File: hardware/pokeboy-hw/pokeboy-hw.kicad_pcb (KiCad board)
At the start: 4 copper layers, 79.4 x 119.4 mm, 110 parts, among them J1 USB Micro-B data/power, J2 LiPo 1S + / NTC / -, J3 POWER SWITCH PADS, J4 8 OHM SPEAKER PADS, J5 EA TFT020-23AINN RGB666, J6 UART TEST PADS, J7 RECOVERY SHORT PADS, J8 RESET SHORT PADS, J9 104031-0811, SW1 EVQ-P1905M, SW2 EVQ-P1905M, SW3 EVQ-P1905M, SW4 EVQ-P1905M, SW5 B3AL-1001P, SW6 B3AL-1001P, SW7 EVQ-P2B02B, SW8 EVQ-P2B02B, U1 OSD3358-1G-ISM, U2 BQ24074RGT, U3 TPS63802DLAR, U4 TPS62162DSG, U5 TPS61165DRV, U6 MAX98357AETE+T, U7 TPD2EUSB30, Y1 24 MHz

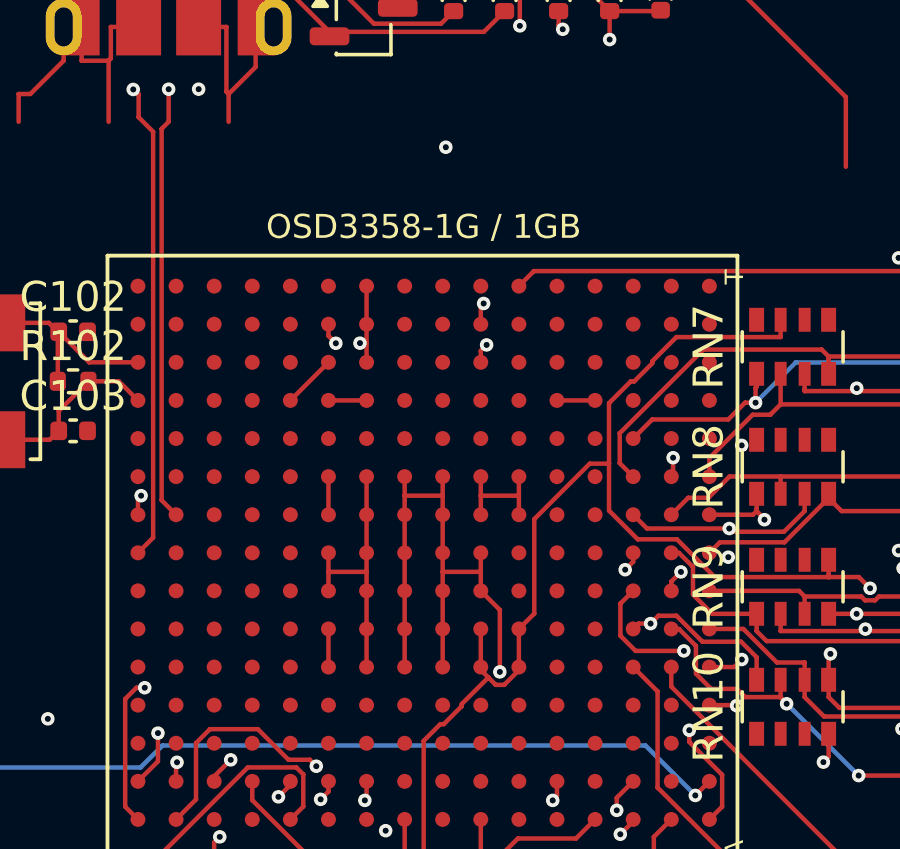
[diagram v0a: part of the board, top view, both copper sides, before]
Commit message: hw: close the Octavo checklist copper items
- SYS_VOUT bulk (PD4, was mandatory-and-missing): C107-C109, three 22 uF 0402
  (same GRM155R61A226ME11D as C7/C8, 66 uF nominal to survive DC-bias derating)
  placed below U1 at y=9.7, fed by a 0.3 mm F.Cu trunk down the col-6/7 ball
  gap from the existing SYS_VOUT interlink; GND pads land in the F.Cu pour.
- VIN_BAT (P8/R8/T8) strapped to PMIC_BAT_SENSE (N7) as new net /VIN_BAT;
  VIN_USB (P9/R9/T9) tied to GND via the N9 ball - Table 13 Use Case 4.
- EEPROM_WP (M2) tied to GND.
- 12 GND stitching vias added beside DGND balls under U1 (was 2 in the whole
  field), each collision-checked on all four layers; drill 227 -> 239 hits.
- U1's schematic symbol gains the 8 previously-floating pins; 3 cap symbols
  added; netlist and board verified identical net for net.

DRC 0 errors / 0 unconnected / 37 warnings (one new cosmetic silk-over-copper
from the cap refs). ERC 0 errors / 4 baseline warnings. Fab outputs, CPL (103
placements), BOM, renders, copper SVGs, STEP, schematic PDF regenerated.

Software note carried in HANDOVER: disable the TPS65217 charger (external
BQ24074 charges the cell) and cap the sustained OPP per the thermal plan.
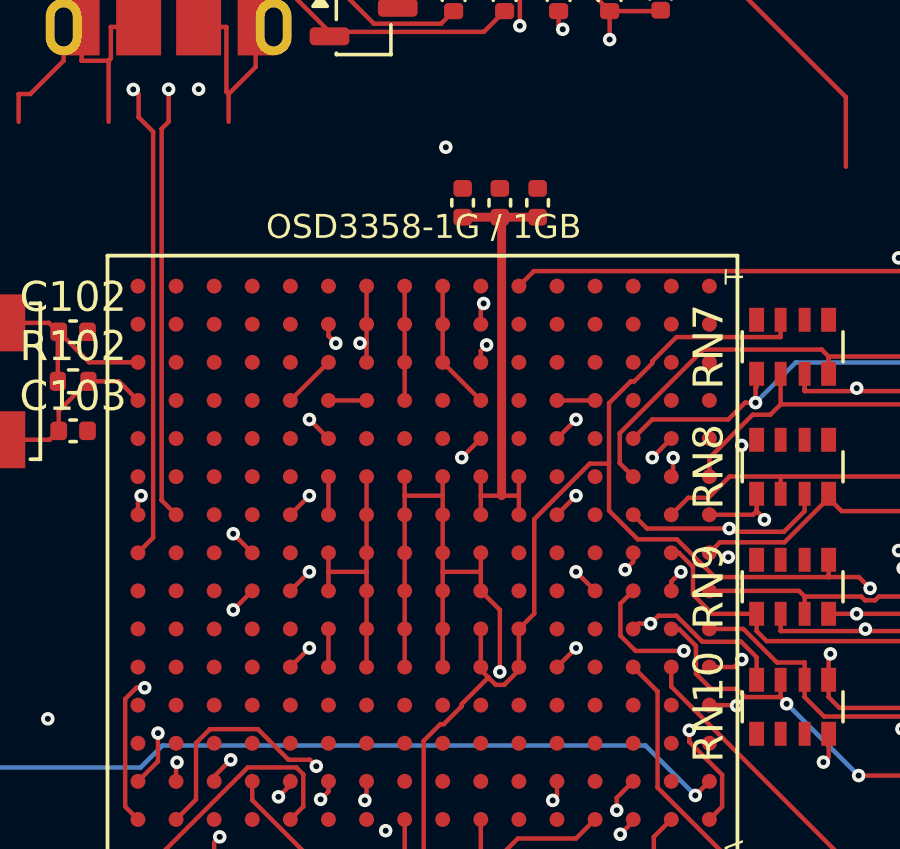
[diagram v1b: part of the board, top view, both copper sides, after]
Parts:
- added C107: 22u/10V, Capacitor_SMD:C_0402_1005Metric, F.Cu at (28.3, 9.70)
- added C108: 22u/10V, Capacitor_SMD:C_0402_1005Metric, F.Cu at (29.5, 9.70)
- added C109: 22u/10V, Capacitor_SMD:C_0402_1005Metric, F.Cu at (30.8, 9.70)
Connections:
- U1 pad M2: (no net) -> /GND
- U1 pad N7: (no net) -> /VIN_BAT
- U1 pad P8: (no net) -> /VIN_BAT
- U1 pad P9: (no net) -> /GND
- U1 pad R8: (no net) -> /VIN_BAT
- U1 pad R9: (no net) -> /GND
- U1 pad T8: (no net) -> /VIN_BAT
- U1 pad T9: (no net) -> /GND
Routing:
- net /GND: track 335.9 -> 350.5 mm, vias 8 -> 20
- net /OSD_SYS: track 3.81 -> 15.6 mm
- net /VIN_BAT: track 0.00 -> 4.34 mm

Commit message: PROTO-B1: fix all design-review findings, DRC/ERC clean
Design review (2026-08-18) found the PROTO-B package unbuildable. All
findings fixed and verified; full record in
hardware/manufacturing/pcbway/OPEN_DESIGN_ISSUES.md.

- U7: TPD2EUSB30DRTR was on a SOT-23-3 land; now Texas_DRT-3, pocket
  re-routed (D+ to In1 below pad 1, D- via In1 spine)
- USB: R1/R2 0R jumpers removed; USB_DP/USB_DM one continuous net per
  leg J1 -> U7 -> U1; stale stubs and redundant vias deleted
- J5: exclude_from_pos_files removed so the WF030-39S FFC connector is
  actually placed (CPL 102 placements); BOM row split connector/panel;
  pin 35 IM3 strap GND -> AUX_3V3 per EA TFT020-23AI RGB mode
- BQ24074: EN1 strap AUX_3V3 -> VBUS; batteryless USB plug-in now
  starts in USB500 instead of deadlocking at USB100
- SYS_VOUT bulk: C107-C109 to 22uF/10V 0805 (GRM21BR61A226ME44L),
  respaced 2.2mm, rail extended (Octavo ~50uF requirement)
- BOM: nonexistent GRM155 22uF MPNs corrected to real GRM158 parts;
  J3/display/switch off-board rows added; MSL 4 stated in fab docs
- RECOVERY net renamed JTAG_TDI (J7 is a TDI test pad; SYSBOOT already
  falls through to USB0 for recovery)
- Y1 resynced from Pokeboy.pretty; silk cleaned to zero warnings;
  mask colour Black in stackup; rev PROTO-B1 on silk and title block

DRC 0 errors / 0 warnings / 0 unconnected; ERC 0 errors.
Full fab regen: gerbers, drills+maps, IPC-D-356, CPL, LAYERS.txt,
PROTO-B1 zips (old PROTO-B zips removed).
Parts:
- removed R1, R2: 0R, Resistor_SMD:R_0402_1005Metric
- C107, C108, C109: footprint Capacitor_SMD:C_0402_1005Metric -> C_0805_2012Metric
- C11, C7, C8: footprint Capacitor_SMD:C_0402_1005Metric -> C_0402_1005Metric
- J5: value EA TFT020-23AINN RGB666 -> EA WF030-39S
- U7: footprint Package_TO_SOT_SMD:SOT-23-3 -> Texas_DRT-3
- Y1: footprint Pokeboy:CRYSTAL_5X3.2MM -> CRYSTAL_5X3.2MM
- moved C109 1.00 mm to (31.8, 9.70)
- moved C107 0.90 mm to (27.4, 9.70)
- moved C108 0.06 mm to (29.6, 9.70)
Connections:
- net /RECOVERY renamed /JTAG_TDI
- J1 pad 2: /USB_DM_CONN -> /USB_DM
- J1 pad 3: /USB_DP_CONN -> /USB_DP
- U7 pad 1: /USB_DP_CONN -> /USB_DP
- U7 pad 2: /USB_DM_CONN -> /USB_DM
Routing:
- net /USB_DM_CONN: track 14.0 -> 0.00 mm
- net /USB_DP_CONN: track 11.2 -> 0.00 mm
- net /USB_DM: track 28.3 -> 32.6 mm
- net /USB_DP: track 30.5 -> 33.8 mm
- net /OSD_SYS: track 15.6 -> 17.5 mm
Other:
- board text added: "0.8 mm 4-LAYER - REV PROTO-B1"
- board text added: "PROTO-B1"
- board text removed: "0.8 mm 4-LAYER - REV PROTO-B"
- board text removed: "PROTO-B / DFM HOLD"
